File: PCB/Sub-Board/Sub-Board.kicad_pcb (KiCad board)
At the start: 4 copper layers, 50.5 x 113 mm, 200 parts, among them J1 Conn_02x08, J10 Type, J11 Power/I2C, J12 Address, J13 Power/I2C, J14 Address, J15 GPIO, J16 Type, J17 GPIO, J18 Type, J19 Power/I2C, J2 Conn_01x04_Pin, J20 Address, J21 Power/I2C, J22 Address, J23 GPIO, J24 Type, J25 GPIO, J26 Type, J27 Power/I2C, J28 Address, J29 Power/I2C, J3 Power/I2C, J30 Address, J31 GPIO, J32 Type, J33 GPIO, J34 Type, J4 Address, J5 Power/I2C, J6 Address, J7 GPIO, J8 Type, J9 GPIO, SW1 SW_DIP_x07, U1 TPS629210DRLR, U2 74HC165, U3 STM32F401VETx, U4 74HC165, U5 74HC165, U6 74HC165, U7 74HC165, Y1 26 MHz

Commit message: Sub Board PCB: More Routing
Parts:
- moved R19 6.03 mm to (148.3, 109.6), turned to 180 degrees
- moved C4 2.91 mm to (121.7, 52.6), turned to 90 degrees
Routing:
- net /STM32-MCU/Slot2.Typ3: track 2.29 -> 49.7 mm
- net /STM32-MCU/Slot7.Typ0: track 2.29 -> 49.1 mm
- net /STM32-MCU/Slot2.Typ2: track 2.29 -> 49.0 mm
- net /STM32-MCU/Slot2.Typ1: track 2.29 -> 48.8 mm
- net /STM32-MCU/Slot2.Typ0: track 2.29 -> 47.8 mm
- net /STM32-MCU/Slot7.Typ1: track 2.29 -> 46.9 mm
- net /STM32-MCU/Slot0.Typ0: track 2.29 -> 46.2 mm
- net /STM32-MCU/Slot0.Typ1: track 2.29 -> 46.2 mm
- net /STM32-MCU/Slot7.Typ2: track 2.29 -> 45.9 mm
- net /STM32-MCU/Slot0.Typ2: track 2.29 -> 45.2 mm
- net /Board Address/BoardAddress5: track 2.28 -> 44.9 mm
- net /Board Address/BoardAddress6: track 2.29 -> 44.5 mm
- net /STM32-MCU/Slot7.Typ3: track 2.29 -> 43.8 mm
- net /Board Address/BoardAddress4: track 2.28 -> 43.3 mm
- net /STM32-MCU/Slot0.Typ3: track 2.29 -> 42.9 mm
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
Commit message: Sub Board PCB: Routing (wip)
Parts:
- moved R5 3.77 mm to (106.2, 115.6), turned to 0 degrees
- moved R19 2.73 mm to (147.1, 112.0), turned to 90 degrees
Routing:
- net /STM32-MCU/Slot4.Typ3: track 2.29 -> 57.0 mm
- net /STM32-MCU/Slot4.Typ2: track 2.29 -> 55.8 mm
- net /STM32-MCU/Slot4.Typ1: track 2.29 -> 55.1 mm
- net /STM32-MCU/Slot4.Typ0: track 2.29 -> 54.7 mm
- net /STM32-MCU/Slot1.Typ3: track 2.29 -> 23.3 mm
- net /STM32-MCU/Slot1.Typ2: track 2.29 -> 21.5 mm
- net /STM32-MCU/Slot1.Typ1: track 2.29 -> 19.8 mm
- net /STM32-MCU/Config.Latch: track 8.64 -> 25.1 mm
- net /STM32-MCU/Slot1.Typ0: track 2.29 -> 18.2 mm
- net Net-(U6-Q7): track 0.00 -> 9.23 mm
- net Net-(U7-Q7): track 0.00 -> 1.50 mm
- net /STM32-MCU/Slot7.Typ3: track 43.8 -> 42.4 mm
- net /STM32-MCU/Slot5.Typ3: track 17.0 -> 15.8 mm
- net /Board Address/BoardAddress5: track 44.9 -> 43.9 mm
- net Net-(U6-CP): track 3.94 -> 3.13 mm
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
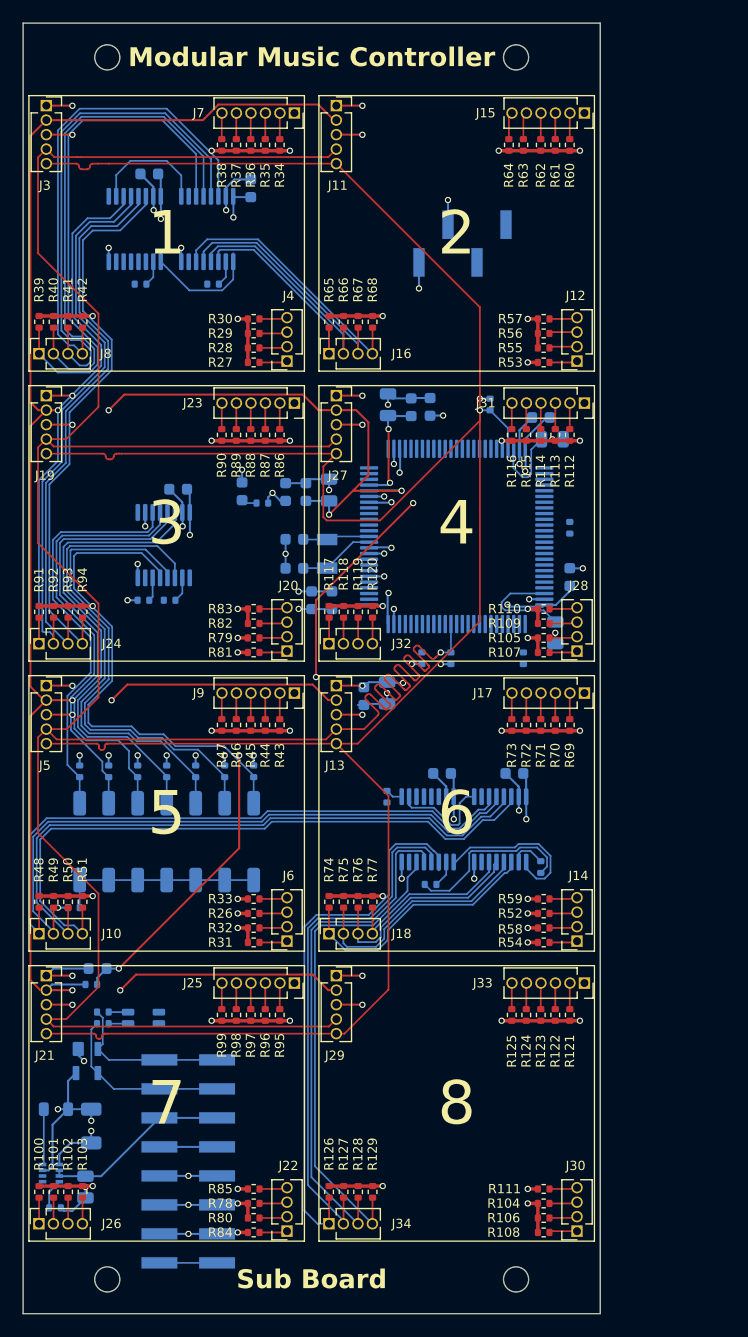
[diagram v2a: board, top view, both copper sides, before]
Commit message: Sub Board PCB: Better component placement
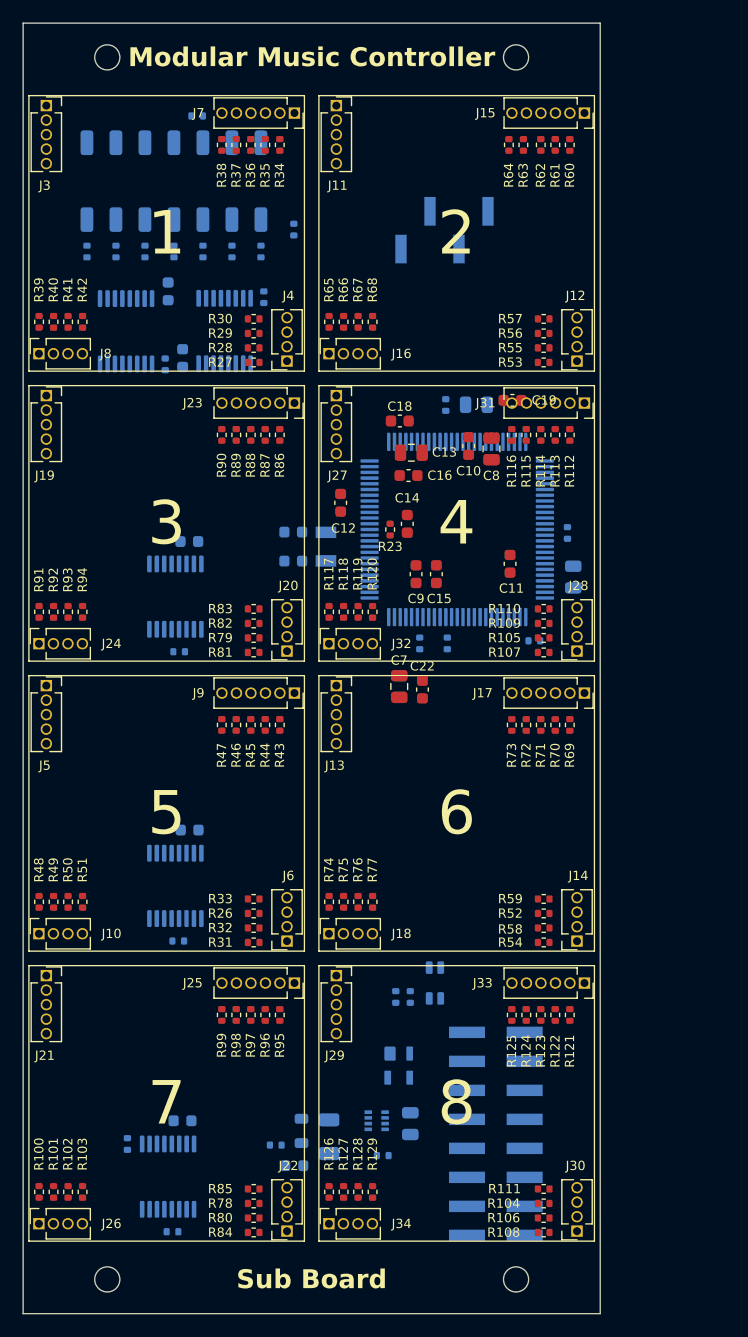
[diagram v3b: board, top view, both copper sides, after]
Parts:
- C10, C11, C12, C13, C14, C15, C16, C18, C19, C22, C7, C8, C9, R23: moved to F.Cu
- moved R5 70.2 mm to (117.0, 46.2)
- moved SW1 57.9 mm to (114.9, 51.9), turned to -90 degrees
- moved R6 48.2 mm to (122.6, 58.1), turned to -90 degrees
- moved R12 47.8 mm to (107.3, 58.1), turned to -90 degrees
- moved R7 46.8 mm to (120.0, 58.1), turned to -90 degrees
- moved R11 46.5 mm to (109.9, 58.1), turned to -90 degrees
- moved R8 45.9 mm to (117.5, 58.1), turned to -90 degrees
- moved R10 45.7 mm to (112.4, 58.1), turned to -90 degrees
- moved R9 45.5 mm to (114.9, 58.1), turned to -90 degrees
- moved C17 38.0 mm to (115.7, 134.2)
- moved R25 38.0 mm to (110.9, 136.3)
- moved U7 38.0 mm to (114.4, 139.1)
- moved R22 37.9 mm to (114.8, 144.0)
- moved R14 34.2 mm to (125.4, 56.2), turned to -90 degrees
- moved R19 32.4 mm to (115.3, 118.5), turned to 0 degrees
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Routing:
- net /STM32-MCU/SlotBus.Clock: track 235.1 -> 0.00 mm, vias 1 -> 0
- net GND: track 228.5 -> 0.00 mm, vias 85 -> 0
- net /STM32-MCU/SlotBus.Data: track 225.1 -> 0.00 mm, vias 1 -> 0
- net /Power Supply/AREF: track 213.4 -> 12.1 mm, vias 8 -> 0
- net /Board Address/+3.3V Digital: track 107.0 -> 0.00 mm, vias 39 -> 0
- net /STM32-MCU/Slot4.Typ3: track 57.0 -> 0.00 mm
- net /STM32-MCU/Slot4.Typ2: track 55.8 -> 0.00 mm
- net /STM32-MCU/Slot4.Typ1: track 55.1 -> 0.00 mm
- net /STM32-MCU/Slot4.Typ0: track 54.7 -> 0.00 mm
- net /Power Supply/+3.3V Analog: track 67.9 -> 13.4 mm, vias 6 -> 0
- net /STM32-MCU/Slot2.Typ3: track 49.7 -> 0.00 mm
- net /STM32-MCU/Slot2.Typ2: track 49.0 -> 0.00 mm
- net /STM32-MCU/Slot2.Typ1: track 48.8 -> 0.00 mm
- net /STM32-MCU/Slot7.Typ0: track 48.5 -> 0.00 mm
- net /STM32-MCU/Slot2.Typ0: track 47.8 -> 0.00 mm
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
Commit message: Sub Board PCB: More routing
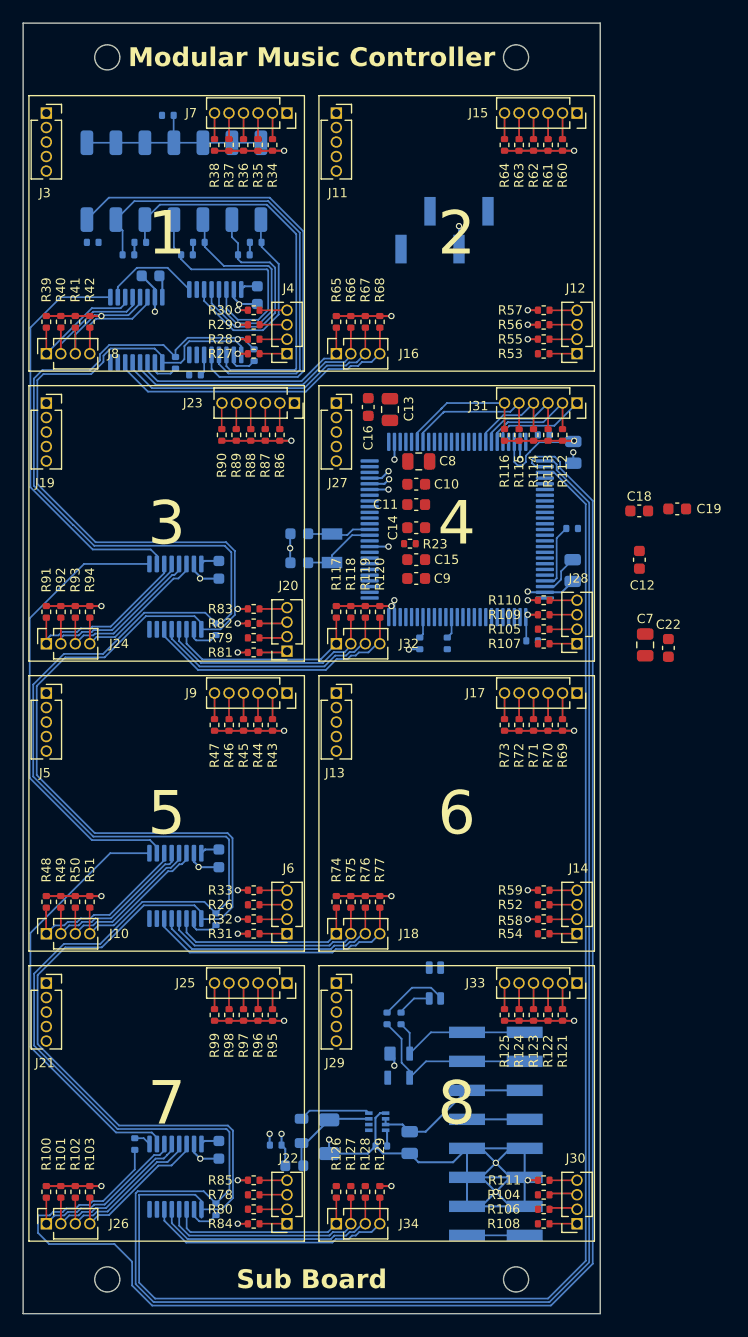
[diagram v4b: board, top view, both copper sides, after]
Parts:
- moved C12 26.6 mm to (155.7, 85.1)
- moved C18 22.4 mm to (155.7, 80.8)
- moved C22 21.8 mm to (158.2, 92.8)
- moved C7 21.8 mm to (156.2, 92.6)
- moved C19 17.3 mm to (159.0, 80.6)
- moved R14 11.5 mm to (122.0, 67.2)
- moved C11 9.72 mm to (136.2, 80.3), turned to 0 degrees
- moved C20 9.45 mm to (149.9, 75.7), turned to -90 degrees
- moved R13 9.09 mm to (116.8, 68.9), turned to 0 degrees
- moved R21 8.97 mm to (147.3, 74.2), turned to 0 degrees
- moved C3 8.56 mm to (122.2, 61.9), turned to -90 degrees
- moved C16 6.96 mm to (132.0, 71.7), turned to -90 degrees
- moved C8 6.47 mm to (136.4, 76.5), turned to 0 degrees
- moved C10 5.68 mm to (136.2, 78.5), turned to 0 degrees
- moved R22 4.29 mm to (118.6, 142.0), turned to -90 degrees
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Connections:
- net Net-(U2-Q7) renamed /STM32-MCU/Config.Out1
- net Net-(U4-Q7) renamed /STM32-MCU/Config.Out2
- net Net-(U5-Q7) renamed /STM32-MCU/Config.Out3
- net Net-(U6-Q7) renamed /STM32-MCU/Config.Out4
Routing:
- net /STM32-MCU/Config.Latch: track 0.00 -> 294.6 mm
- net /STM32-MCU/Config.Clock: track 0.00 -> 294.1 mm
- net /Power Supply/AREF: track 12.1 -> 226.0 mm, vias 0 -> 2
- net GND: track 0.00 -> 205.9 mm, vias 0 -> 55
- net /STM32-MCU/Config.Data: track 0.00 -> 143.1 mm
- net /Power Supply/+3.3V Analog: track 13.4 -> 137.4 mm, vias 0 -> 2
- net /Board Address/BoardAddress6: track 0.00 -> 43.0 mm
- net /Board Address/BoardAddress5: track 0.00 -> 41.6 mm
- net /STM32-MCU/Config.Out3: track 0.00 -> 40.6 mm
- net /STM32-MCU/Config.Out4: track 0.00 -> 38.2 mm
- net /STM32-MCU/Config.Out2: track 0.00 -> 36.4 mm
- net /Board Address/BoardAddress4: track 0.00 -> 36.0 mm
- net /STM32-MCU/Slot1.Typ3: track 0.00 -> 27.3 mm
- net /STM32-MCU/Slot1.Typ2: track 0.00 -> 25.2 mm
- net /STM32-MCU/Slot3.Typ3: track 0.00 -> 23.9 mm
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- added copper zone on In1.Cu, net GND

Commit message: Sub Board PCB: Slot2 routing
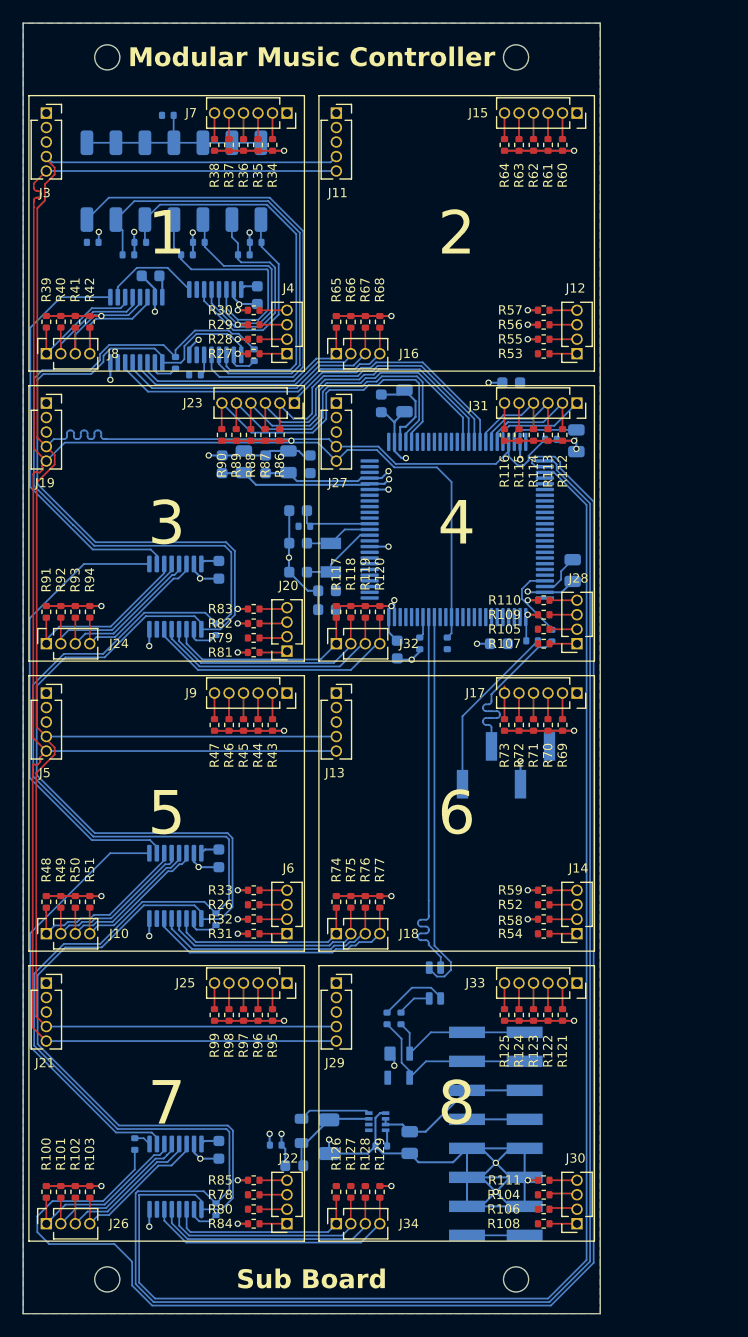
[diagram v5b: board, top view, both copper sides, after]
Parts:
- C10, C11, C12, C13, C14, C15, C16, C18, C19, C22, C7, C8, C9, R23: moved to B.Cu
- moved J2 47.2 mm to (144.0, 103.1)
- moved C22 33.0 mm to (133.1, 71.4)
- moved C7 30.0 mm to (135.1, 71.2)
- moved C18 24.4 mm to (134.5, 93.0), turned to -90 degrees
- moved C19 19.6 mm to (143.4, 92.5)
- moved C12 19.1 mm to (144.5, 69.6), turned to 180 degrees
- moved C16 13.7 mm to (119.2, 76.7), turned to 90 degrees
- moved C9 13.6 mm to (126.9, 76.7), turned to 90 degrees
- moved C13 13.6 mm to (121.1, 76.5), turned to 90 degrees
- moved C10 13.3 mm to (123.0, 76.7), turned to 90 degrees
- moved C8 11.4 mm to (125.0, 76.5), turned to 90 degrees
- moved C11 10.9 mm to (128.3, 87.8), turned to 180 degrees
- moved C14 10.5 mm to (125.8, 80.8), turned to 180 degrees
- moved R16 9.55 mm to (148.0, 91.7), turned to -90 degrees
- moved R23 9.37 mm to (126.4, 82.2), turned to 0 degrees
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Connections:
- J11 pad 4: /STM32-MCU/SlotBus.Clock -> /STM32-MCU/SlotBus.Data
- J11 pad 5: /STM32-MCU/SlotBus.Data -> /STM32-MCU/SlotBus.Clock
- J13 pad 4: /STM32-MCU/SlotBus.Clock -> /STM32-MCU/SlotBus.Data
- J13 pad 5: /STM32-MCU/SlotBus.Data -> /STM32-MCU/SlotBus.Clock
- J19 pad 4: /STM32-MCU/SlotBus.Clock -> /STM32-MCU/SlotBus.Data
- J19 pad 5: /STM32-MCU/SlotBus.Data -> /STM32-MCU/SlotBus.Clock
- J21 pad 4: /STM32-MCU/SlotBus.Clock -> /STM32-MCU/SlotBus.Data
- J21 pad 5: /STM32-MCU/SlotBus.Data -> /STM32-MCU/SlotBus.Clock
- J27 pad 4: /STM32-MCU/SlotBus.Clock -> /STM32-MCU/SlotBus.Data
- J27 pad 5: /STM32-MCU/SlotBus.Data -> /STM32-MCU/SlotBus.Clock
- J29 pad 4: /STM32-MCU/SlotBus.Clock -> /STM32-MCU/SlotBus.Data
- J29 pad 5: /STM32-MCU/SlotBus.Data -> /STM32-MCU/SlotBus.Clock
- J3 pad 4: /STM32-MCU/SlotBus.Clock -> /STM32-MCU/SlotBus.Data
- J3 pad 5: /STM32-MCU/SlotBus.Data -> /STM32-MCU/SlotBus.Clock
- J5 pad 4: /STM32-MCU/SlotBus.Clock -> /STM32-MCU/SlotBus.Data
- J5 pad 5: /STM32-MCU/SlotBus.Data -> /STM32-MCU/SlotBus.Clock
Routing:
- net /STM32-MCU/SlotBus.Data: track 0.00 -> 209.3 mm
- net /STM32-MCU/SlotBus.Clock: track 1.95 -> 208.8 mm
- net GND: track 205.9 -> 244.0 mm, vias 55 -> 67
- net /STM32-MCU/SystemBus.Clock: track 0.00 -> 34.0 mm
- net /STM32-MCU/SystemBus.Data: track 0.00 -> 33.9 mm
- net /STM32-MCU/Slot2.A0: track 2.29 -> 29.6 mm
- net /STM32-MCU/Slot2.A: track 2.29 -> 28.8 mm
- net /STM32-MCU/Slot2.A1: track 2.29 -> 28.6 mm
- net /STM32-MCU/Slot2.B: track 2.29 -> 28.0 mm
- net /STM32-MCU/Slot2.C: track 2.29 -> 27.2 mm
- net /STM32-MCU/Slot2.LED: track 0.00 -> 21.9 mm
- net /STM32-MCU/SWCLK: track 0.00 -> 15.3 mm
- net /STM32-MCU/SWDIO: track 0.00 -> 15.2 mm
- net /STM32-MCU/Slot3.A1: track 12.7 -> 2.27 mm
- net /Board Address/+3.3V Digital: track 17.3 -> 27.6 mm
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- added copper zone on B.Cu, net /Board Address/+3.3V Digital
- removed copper zone on In1.Cu, net /Board Address/+3.3V Digital

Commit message: Sub Board PCB: Slot routing (wip)
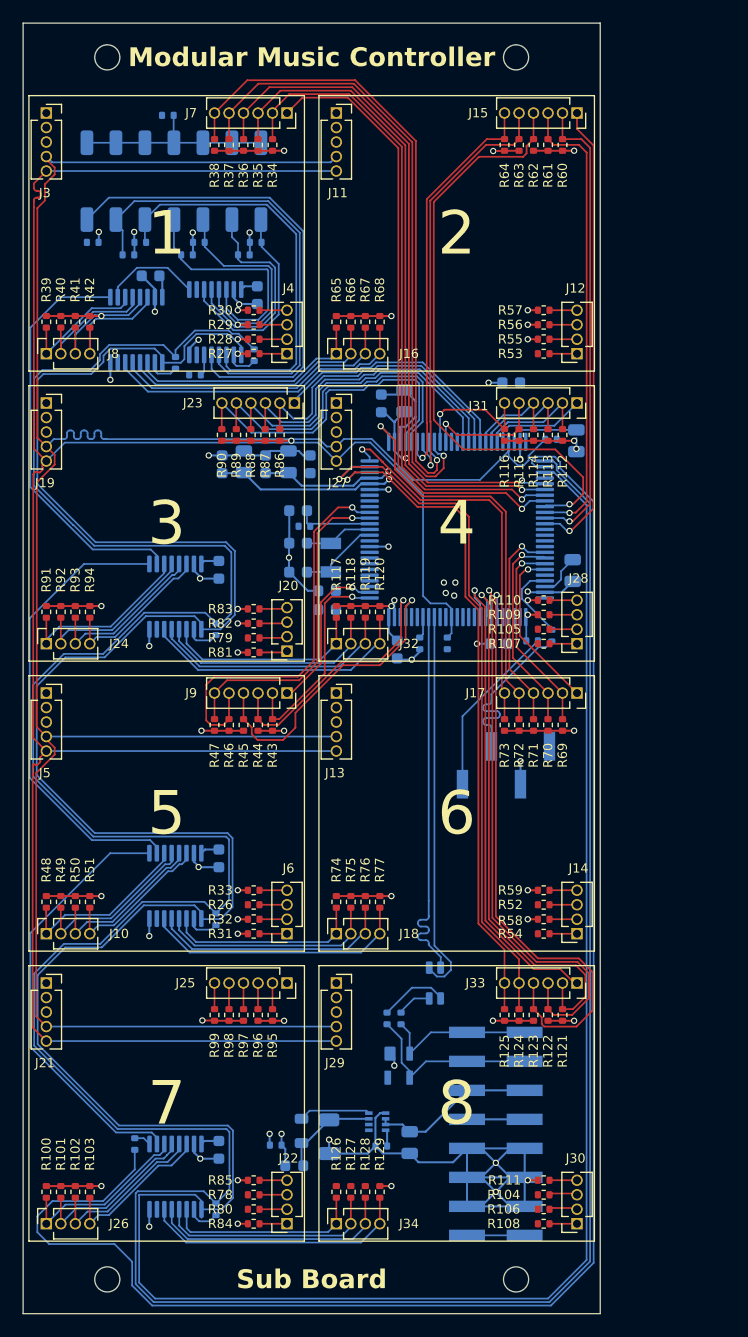
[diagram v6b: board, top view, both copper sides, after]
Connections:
- U3 pad 1: /STM32-MCU/Slot0.C -> /STM32-MCU/Slot4.C
- U3 pad 15: /STM32-MCU/Slot5.A0 -> /STM32-MCU/Slot4.A0
- U3 pad 16: /STM32-MCU/Slot5.A1 -> /STM32-MCU/Slot4.A1
- U3 pad 2: /STM32-MCU/Slot0.LED -> /STM32-MCU/Slot4.LED
- U3 pad 23: /STM32-MCU/Slot0.A0 -> /STM32-MCU/Slot7.A0
- U3 pad 24: /STM32-MCU/Slot0.A1 -> /STM32-MCU/Slot7.A1
- U3 pad 25: /STM32-MCU/Slot1.A0 -> /STM32-MCU/Slot5.A0
- U3 pad 26: /STM32-MCU/Slot1.A1 -> /STM32-MCU/Slot5.A1
- U3 pad 3: /STM32-MCU/Slot1.A -> unconnected-(U3-PE4-Pad3)
- U3 pad 31: /STM32-MCU/Slot3.A0 -> /STM32-MCU/Slot1.A0
- U3 pad 32: /STM32-MCU/Slot3.A1 -> /STM32-MCU/Slot1.A1
- U3 pad 33: /STM32-MCU/Slot7.A0 -> /STM32-MCU/Slot0.A0
- U3 pad 34: /STM32-MCU/Slot7.A1 -> /STM32-MCU/Slot0.A1
- U3 pad 35: /STM32-MCU/Slot4.A0 -> /STM32-MCU/Slot3.A0
- U3 pad 36: /STM32-MCU/Slot4.A1 -> /STM32-MCU/Slot3.A1
- U3 pad 38: /STM32-MCU/Slot1.LED -> unconnected-(U3-PE7-Pad38)
- U3 pad 4: /STM32-MCU/Slot1.B -> unconnected-(U3-PE5-Pad4)
- U3 pad 5: /STM32-MCU/Slot1.C -> unconnected-(U3-PE6-Pad5)
- U3 pad 55: /STM32-MCU/Slot6.A -> /STM32-MCU/Slot0.A
- U3 pad 56: /STM32-MCU/Slot6.B -> /STM32-MCU/Slot0.B
- U3 pad 57: /STM32-MCU/Slot6.C -> /STM32-MCU/Slot0.C
- U3 pad 58: /STM32-MCU/Slot6.LED -> /STM32-MCU/Slot0.LED
- U3 pad 59: /STM32-MCU/Slot7.A -> /STM32-MCU/Slot1.A
- U3 pad 60: /STM32-MCU/Slot7.B -> /STM32-MCU/Slot1.B
- U3 pad 61: /STM32-MCU/Slot7.C -> /STM32-MCU/Slot1.C
- U3 pad 62: /STM32-MCU/Slot7.LED -> /STM32-MCU/Slot1.LED
- U3 pad 67: unconnected-(U3-PA8-Pad67) -> /STM32-MCU/Slot5.A
- U3 pad 68: unconnected-(U3-PA9-Pad68) -> /STM32-MCU/Slot5.B
- U3 pad 69: unconnected-(U3-PA10-Pad69) -> /STM32-MCU/Slot5.C
- U3 pad 70: unconnected-(U3-PA11-Pad70) -> /STM32-MCU/Slot5.LED
- U3 pad 81: /STM32-MCU/Slot4.A -> /STM32-MCU/Slot7.A
- U3 pad 82: /STM32-MCU/Slot4.B -> /STM32-MCU/Slot7.B
- U3 pad 83: /STM32-MCU/Slot4.C -> /STM32-MCU/Slot7.C
- U3 pad 84: /STM32-MCU/Slot4.LED -> /STM32-MCU/Slot7.LED
- U3 pad 85: /STM32-MCU/Slot5.A -> /STM32-MCU/Slot6.A
- U3 pad 86: /STM32-MCU/Slot5.B -> /STM32-MCU/Slot6.B
- U3 pad 87: /STM32-MCU/Slot5.C -> /STM32-MCU/Slot6.C
- U3 pad 88: /STM32-MCU/Slot5.LED -> /STM32-MCU/Slot6.LED
- U3 pad 97: /STM32-MCU/Slot0.A -> /STM32-MCU/Slot4.A
- U3 pad 98: /STM32-MCU/Slot0.B -> /STM32-MCU/Slot4.B
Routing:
- net /STM32-MCU/Slot7.A1: track 2.27 -> 61.7 mm, vias 0 -> 1
- net /STM32-MCU/Slot0.A: track 2.27 -> 60.5 mm, vias 0 -> 1
- net /STM32-MCU/Slot0.B: track 2.27 -> 59.1 mm, vias 0 -> 1
- net /STM32-MCU/Slot7.A0: track 2.27 -> 58.9 mm, vias 0 -> 1
- net /STM32-MCU/Slot0.C: track 2.27 -> 58.2 mm, vias 0 -> 1
- net /STM32-MCU/Slot0.LED: track 0.00 -> 54.8 mm, vias 0 -> 1
- net /STM32-MCU/Slot0.A0: track 2.27 -> 56.5 mm, vias 0 -> 1
- net /STM32-MCU/Slot0.A1: track 2.27 -> 56.1 mm, vias 0 -> 1
- net /STM32-MCU/Slot1.A: track 2.27 -> 53.3 mm, vias 0 -> 1
- net /STM32-MCU/Slot7.A: track 2.31 -> 53.0 mm, vias 0 -> 1
- net /STM32-MCU/Slot7.B: track 2.31 -> 50.5 mm, vias 0 -> 1
- net /STM32-MCU/Slot7.C: track 2.27 -> 48.1 mm, vias 0 -> 1
- net /STM32-MCU/Slot7.LED: track 0.06 -> 42.3 mm, vias 0 -> 1
- net /STM32-MCU/Slot1.LED: track 0.00 -> 40.6 mm, vias 0 -> 1
- net /STM32-MCU/Slot1.C: track 2.27 -> 41.1 mm, vias 0 -> 1
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- removed copper zone on B.Cu, net /Board Address/+3.3V Digital
